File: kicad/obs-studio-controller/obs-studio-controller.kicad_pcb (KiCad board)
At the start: 2 copper layers, 111 x 113.8 mm, 70 parts, among them J1 PWR_SWITCH, J2 EXT_PWR, J3 LEDS, J4 Conn_Display, J5 BUTTONS, J6 GPIO, J7 WS2812, Q1 2N7002, Q2 SS8050_C2150, Q3 SS8050_C2150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

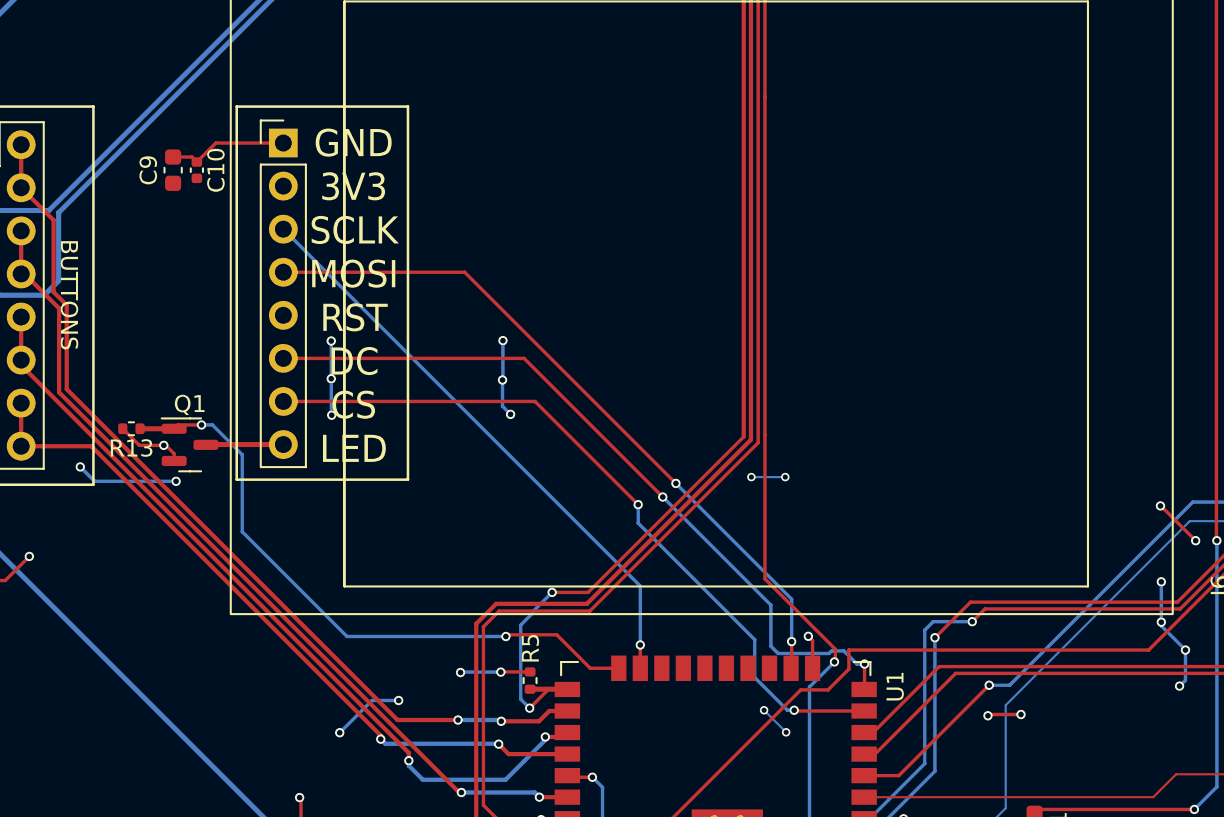
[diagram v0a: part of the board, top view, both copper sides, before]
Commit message: Fix flipped display header
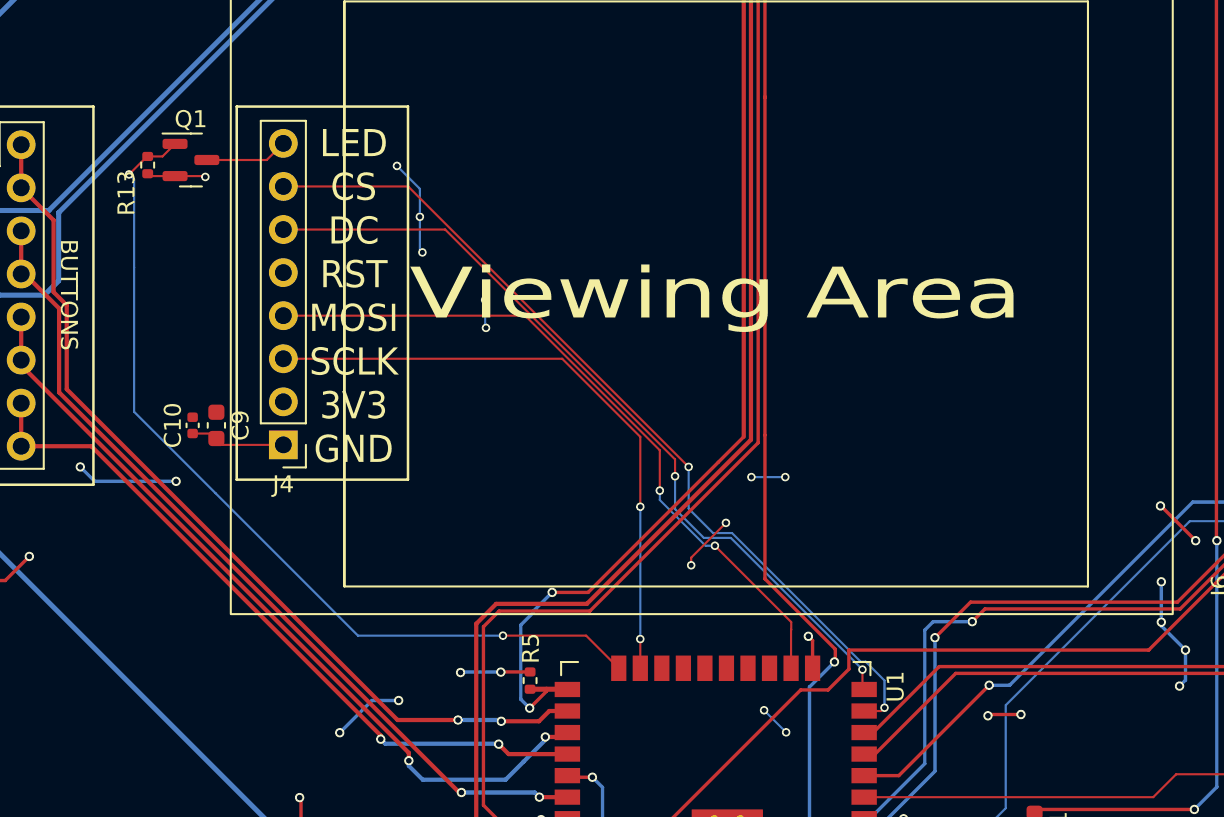
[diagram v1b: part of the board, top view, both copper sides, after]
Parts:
- moved Q1 16.8 mm to (16.6, 18.9)
- moved R13 15.6 mm to (14.0, 19.2), turned to -90 degrees
- moved C9 15.3 mm to (18.1, 34.5), turned to -90 degrees
- moved C10 15.1 mm to (16.6, 34.6), turned to 90 degrees
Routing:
- net /DISPLAY_LED: track 37.0 -> 52.4 mm
- net /DISPLAY_CS: track 43.8 -> 51.8 mm
- net /DISPLAY_DC: track 44.8 -> 47.8 mm
- net GND: track 108.1 -> 106.0 mm
- net /DISPLAY_SCLK: track 34.6 -> 36.6 mm, vias 1 -> 2
- net +3V3: track 75.5 -> 77.3 mm, vias 40 -> 41
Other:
- board text added: "LED CS DC RST MOSI SCLK 3V3 GND"
- board text removed: "GND 3V3 SCLK MOSI RST DC CS LED"

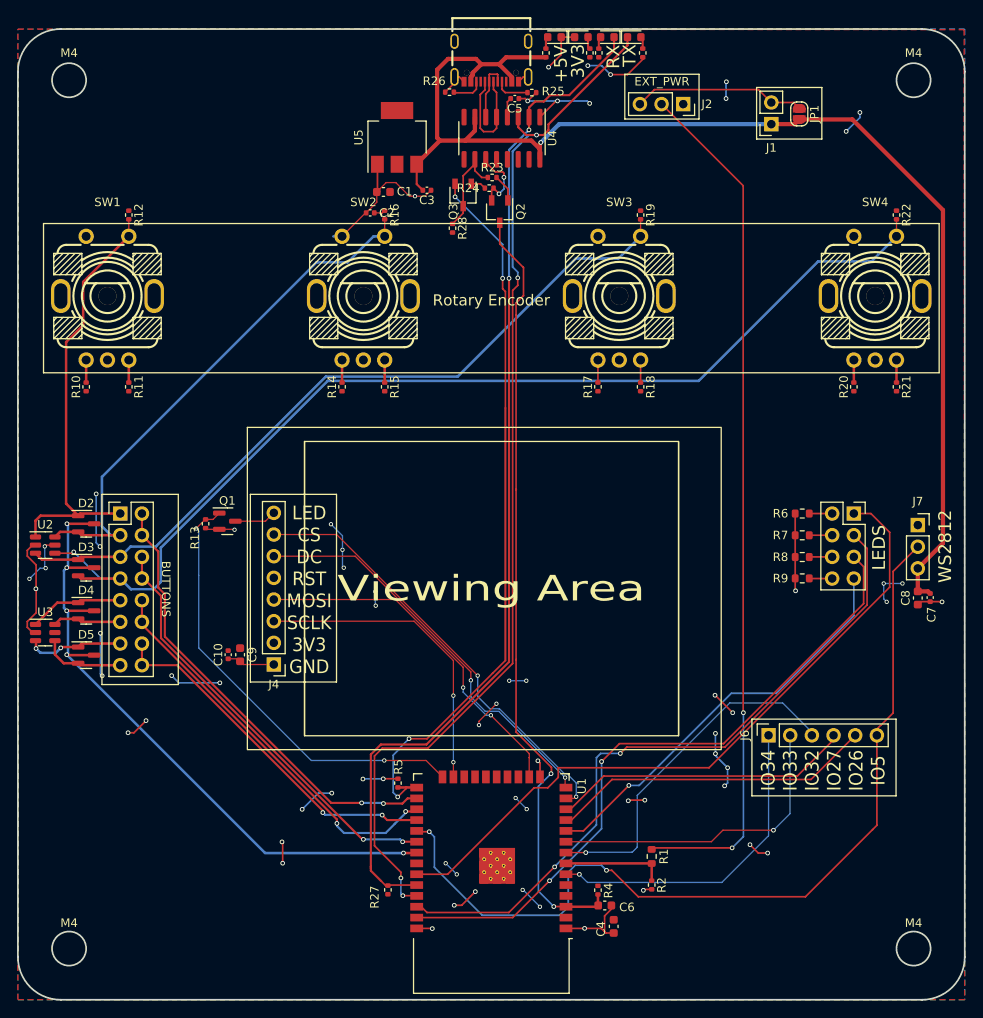
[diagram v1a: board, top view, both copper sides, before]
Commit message: Actually connect rotary encoder
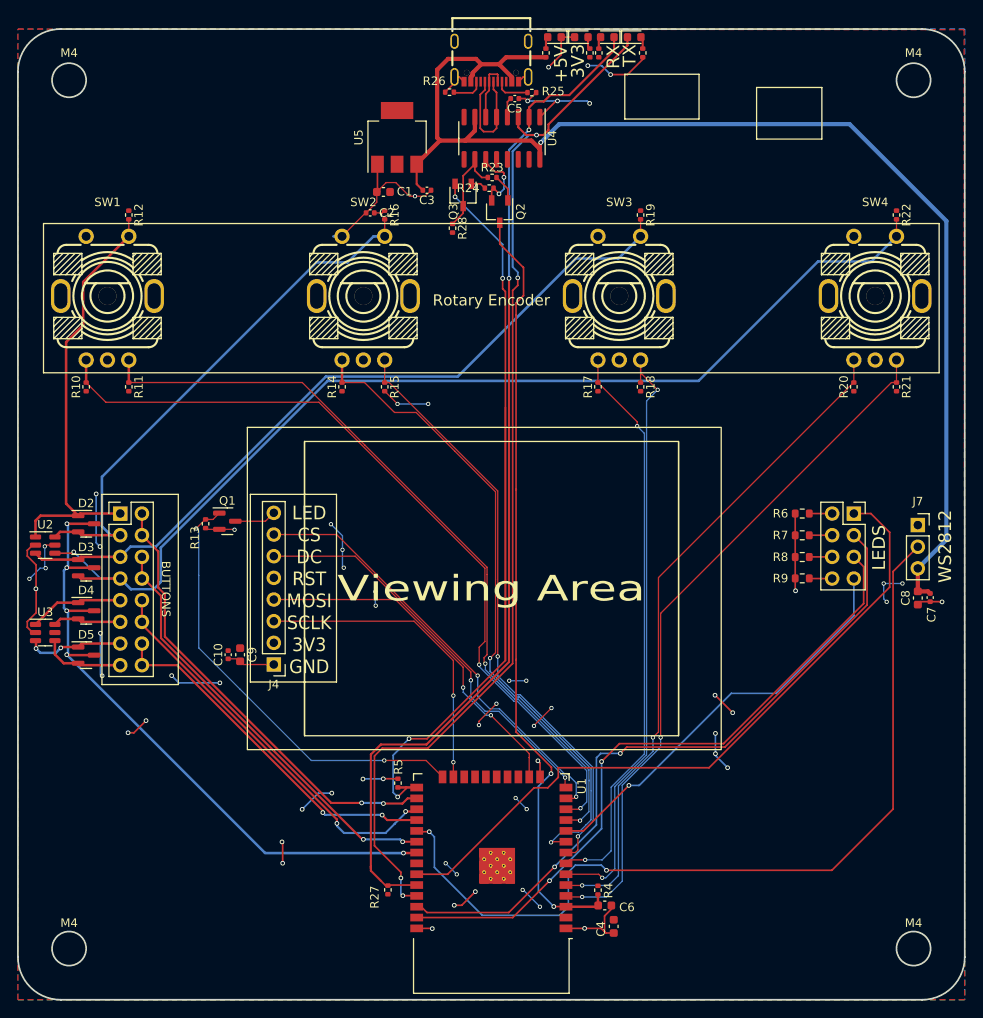
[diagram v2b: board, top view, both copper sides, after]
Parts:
- removed J1: PWR_SWITCH, Connector_PinSocket_2.54mm:PinSocket_1x02_P2.54mm_Vertical
- removed J2: EXT_PWR, Connector_PinSocket_2.54mm:PinSocket_1x03_P2.54mm_Vertical
- removed J6: GPIO, Connector_PinSocket_2.54mm:PinSocket_1x06_P2.54mm_Vertical
- removed JP1: SolderJumper_2_Open, Jumper:SolderJumper-2_P1.3mm_Open_RoundedPad1.0x1.5mm
- removed R1: 30k, Resistor_SMD:R_0603_1608Metric
- removed R2: 100k, Resistor_SMD:R_0402_1005Metric
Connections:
- U1 pad 11: /IO26 -> /ROT1_CLK
- U1 pad 12: /IO27 -> /ROT1_DT
- U1 pad 4: unconnected-(U1-Pad4) -> /ROT4_CLK
- U1 pad 5: unconnected-(U1-Pad5) -> /ROT4_DT
- U1 pad 6: /IO34 -> /ROT3_CLK
- U1 pad 7: /EXT_SENSE -> /ROT3_DT
- U1 pad 8: /IO32 -> /ROT2_CLK
- U1 pad 9: /IO33 -> /ROT2_DT
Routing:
- net /EXT_MONITOR: track 101.2 -> 0.00 mm, vias 2 -> 0
- net /ROT1_DT: track 2.64 -> 94.3 mm, vias 0 -> 2
- net /ROT1_CLK: track 2.64 -> 90.9 mm, vias 0 -> 2
- net /ROT4_CLK: track 2.64 -> 82.2 mm, vias 0 -> 2
- net /ROT4_DT: track 2.64 -> 78.6 mm, vias 0 -> 2
- net /ROT2_DT: track 2.64 -> 77.4 mm, vias 0 -> 2
- net /ROT3_CLK: track 2.64 -> 71.5 mm, vias 0 -> 2
- net /ROT2_CLK: track 2.64 -> 70.4 mm, vias 0 -> 2
- net /ROT3_DT: track 2.64 -> 67.3 mm, vias 0 -> 2
- net /IO32: track 41.5 -> 0.00 mm, vias 1 -> 0
- net /IO34: track 38.2 -> 0.00 mm, vias 1 -> 0
- net /IO26: track 38.0 -> 0.00 mm
- net /IO33: track 36.8 -> 0.00 mm, vias 1 -> 0
- net /IO27: track 35.3 -> 0.00 mm
- net /VEXT: track 20.3 -> 0.00 mm
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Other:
- board text removed: "IO34 IO33 IO32 IO27 IO26 IO5"

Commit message: Forgot to add 3v3 trace
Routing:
- net +3V3: track 75.8 -> 82.7 mm, vias 38 -> 40
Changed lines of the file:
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@@
   (gr_rect (start 19.25 15.8) (end 29.35 37.8) (layer "B.SilkS") (width 0.15) (fill none))
   (gr_rect (start 1.85 15.75) (end 10.8 38.05) (layer "F.SilkS") (width 0.15) (fill none))
-  (gr_rect (start 78.6 -31.95) (end 86.25 -25.9) (layer "F.SilkS") (width 0.15) (fill none))
-  (gr_rect (start 63.15 -28.25) (end 71.85 -33.5) (layer "F.SilkS") (width 0.15) (fill none))
   (gr_rect (start 19.25 15.75) (end 29.35 37.75) (layer "F.SilkS") (width 0.15) (fill none))
   (gr_rect (start -5 -16) (end 100 1.5) (layer "F.SilkS") (width 0.15) (fill none))
@@
   (segment (start 61.85 65.625) (end 61.59 65.365) (width 0.3) (layer "F.Cu") (net 2))
   (segment (start 30.015 3.675) (end 30 3.66) (width 0.3) (layer "F.Cu") (net 2))
+  (segment (start 3.19 3.66) (end 3.05 3.8) (width 0.127) (layer "F.Cu") (net 2))
   (segment (start 35.01 3.66) (end 36.5 5.15) (width 0.127) (layer "F.Cu") (net 2))
   (segment (start 63.46 -33.46) (end 65.25 -35.25) (width 0.2) (layer "F.Cu") (net 2))
   (segment (start 34.74 -17.25) (end 35 -17.51) (width 0.127) (layer "F.Cu") (net 2))
   (segment (start 4.985 3.675) (end 5 3.66) (width 0.3) (layer "F.Cu") (net 2))
+  (segment (start 0.35 5.1) (end 0 4.75) (width 0.127) (layer "F.Cu") (net 2))
   (segment (start 35 3.66) (end 35.01 3.66) (width 0.127) (layer "F.Cu") (net 2))
+  (segment (start 0 4.75) (end 0 3.66) (width 0.127) (layer "F.Cu") (net 2))
   (segment (start 90.015 3.675) (end 90 3.66) (width 0.3) (layer "F.Cu") (net 2))
   (segment (start 48.1 40.3) (end 46.05 42.35) (width 0.127) (layer "F.Cu") (net 2))
@@
   (segment (start -3.6625 21.7) (end -4.7 21.7) (width 0.127) (layer "F.Cu") (net 2))
   (segment (start 61.48 -33.46) (end 63.46 -33.46) (width 0.2) (layer "F.Cu") (net 2))
+  (segment (start 5 3.66) (end 3.19 3.66) (width 0.127) (layer "F.Cu") (net 2))
+  (via (at 3.05 3.8) (size 0.5) (drill 0.3) (layers "F.Cu" "B.Cu") (net 2))
   (via (at 61.48 -33.46) (size 0.55) (drill 0.33) (layers "F.Cu" "B.Cu") (free) (net 2))
   (via (at -6.65 25.65) (size 0.5) (drill 0.3) (layers "F.Cu" "B.Cu") (net 2))
@@
   (via (at 43.45 60.3) (size 0.5) (drill 0.3) (layers "F.Cu" "B.Cu") (net 2))
   (via (at 1.875 37.025) (size 0.55) (drill 0.33) (layers "F.Cu" "B.Cu") (net 2))
+  (via (at 0.35 5.1) (size 0.5) (drill 0.3) (layers "F.Cu" "B.Cu") (net 2))
   (via (at 51.6 37.6) (size 0.5) (drill 0.3) (layers "F.Cu" "B.Cu") (free) (net 2))
   (via (at -4.85 21.85) (size 0.5) (drill 0.3) (layers "F.Cu" "B.Cu") (net 2))
@@
   (segment (start 42.15 59) (end 43.45 60.3) (width 0.127) (layer "B.Cu") (net 2))
   (segment (start -4.75 24.4) (end -5.4 24.4) (width 0.127) (layer "B.Cu") (net 2))
+  (segment (start 3.05 3.8) (end 1.65 3.8) (width 0.127) (layer "B.Cu") (net 2))
   (segment (start 36.5 5.15) (end 40.1 5.15) (width 0.127) (layer "B.Cu") (net 2))
   (segment (start 93.5 28) (end 93.85 28.35) (width 0.127) (layer "B.Cu") (net 2))
@@
   (segment (start 1.675 32.025) (end 1.675 36.825) (width 0.2) (layer "B.Cu") (net 2))
   (segment (start 34.825 49.1) (end 32.475 49.1) (width 0.2) (layer "B.Cu") (net 2))
+  (segment (start 1.65 3.8) (end 0.35 5.1) (width 0.127) (layer "B.Cu") (net 2))
   (segment (start -5.4 24.4) (end -6.65 25.65) (width 0.127) (layer "B.Cu") (net 2))
   (segment (start 30.05 24.2) (end 30.05 22.25) (width 0.127) (layer "B.Cu") (net 2))

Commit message: Updated pcb
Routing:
- net +3V3: track 82.7 -> 132.9 mm, vias 40 -> 48
- net GND: track 103.5 -> 114.9 mm
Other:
- board text added: "V2.2"
- board text added: "https://github.com/CommanderRedYT/obs-studio-controller/"

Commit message: Updated for production
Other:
- board text added: "V2.2 (d970e1112e0216fa4e93fd7c06fc8bf963436747)"
- board text removed: "V2.2"
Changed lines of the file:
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@@
     (effects (font (size 1.5 1.5) (thickness 0.3)))
   )
-  (gr_text "V2.2" (at -3.7 -36.825) (layer "F.SilkS")
-    (effects (font (size 1.5 1.5) (thickness 0.3) bold) (justify left bottom))
+  (gr_text "V2.2 (d970e1112e0216fa4e93fd7c06fc8bf963436747)" (at -3.65 -37.2) (layer "F.SilkS")
+    (effects (font (size 1 1) (thickness 0.2)) (justify left bottom))
   )
   (gr_text "+5V" (at 55.65 -34.7 90) (layer "F.SilkS")
